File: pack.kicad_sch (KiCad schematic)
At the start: 34 parts

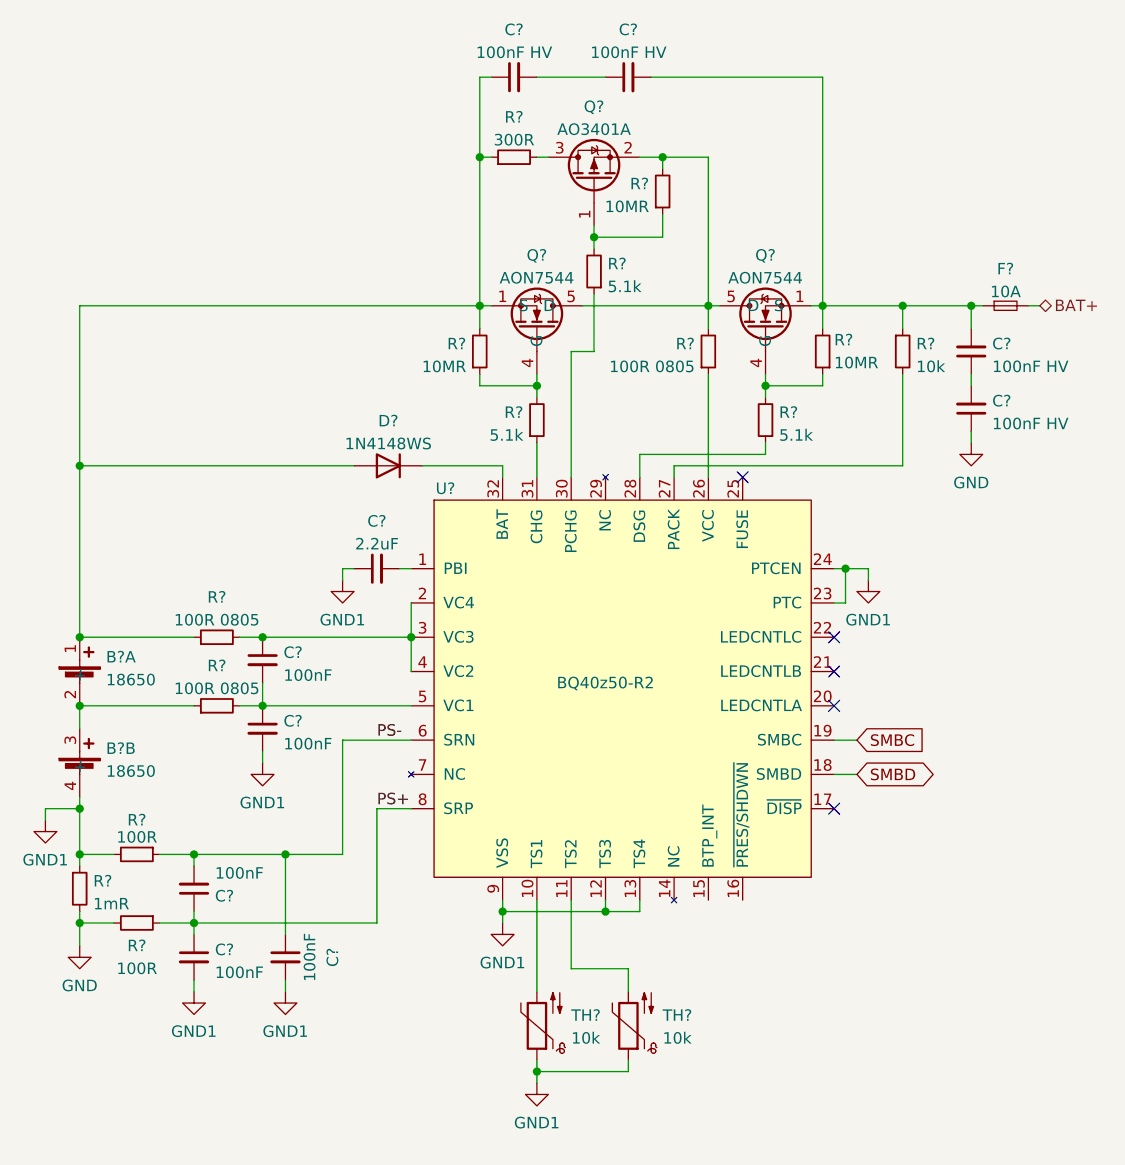
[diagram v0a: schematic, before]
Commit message: Add individually switchable outputs
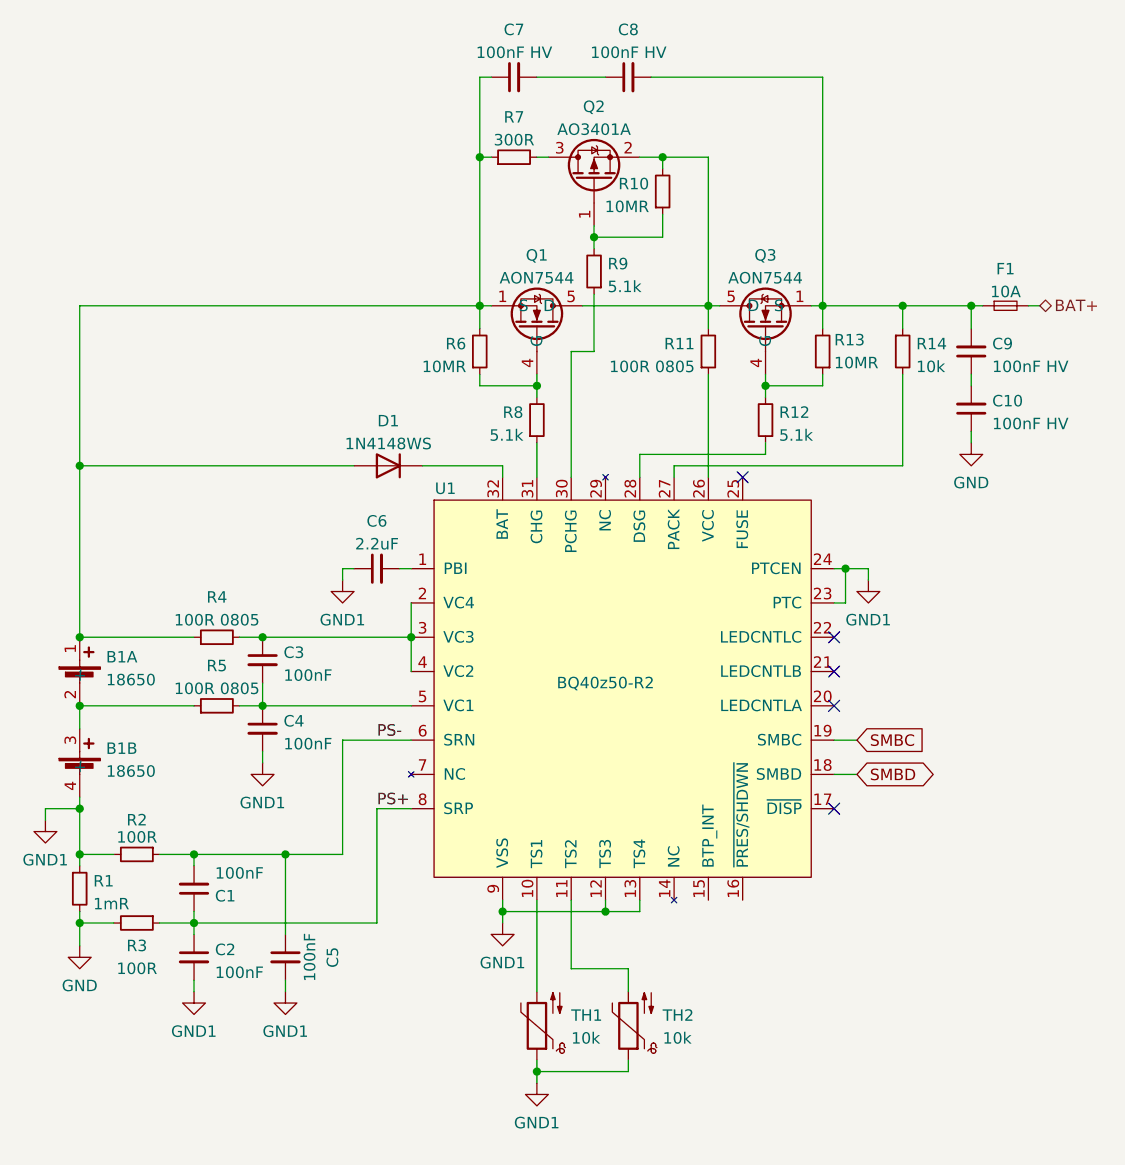
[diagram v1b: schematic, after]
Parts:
- gave numbers to parts that had none: 33

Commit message: Finish step-up component placement and partial layout
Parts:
- added R95: 10k, Resistor_SMD:R_0402_1005Metric, symbol Device:R_Small
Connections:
- net GND1: now also R95.2
- net at U1.16 (~{PRES/SHDWN}): now also R95.1
- no-connect marks 5 -> 6
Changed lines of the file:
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@@
   (no_connect (at 158.75 118.11))
   (no_connect (at 148.59 81.28))
+  (no_connect (at 144.78 128.27))
   (no_connect (at 158.75 99.06))
   (no_connect (at 158.75 106.68))
@@
     (stroke (width 0) (type default) (color 0 0 0 0))
   )
+  (wire (pts (xy 148.59 128.27) (xy 148.59 129.54))
+    (stroke (width 0) (type default) (color 0 0 0 0))
+  )
   (wire (pts (xy 121.92 80.01) (xy 121.92 81.28))
     (stroke (width 0) (type default) (color 0 0 0 0))
@@
   )
   (wire (pts (xy 87.63 137.16) (xy 87.63 138.43))
+    (stroke (width 0) (type default) (color 0 0 0 0))
+  )
+  (wire (pts (xy 148.59 134.62) (xy 148.59 135.89))
     (stroke (width 0) (type default) (color 0 0 0 0))
   )
@@
   (hierarchical_label "BAT+" (shape bidirectional) (at 181.61 62.23 0)
     (effects (font (size 1.27 1.27)) (justify left))
+  )
+  (symbol (lib_id "Device:R_Small") (at 148.59 132.08 0) (unit 1)
+    (in_bom yes) (on_board yes) (fields_autoplaced)
+    (property "Reference" "R95" (id 0) (at 150.0886 131.2453 0)
+      (effects (font (size 1.27 1.27)) (justify left))
+    )
+    (property "Value" "10k" (id 1) (at 150.0886 133.7822 0)
+      (effects (font (size 1.27 1.27)) (justify left))
+    )
+    (property "Footprint" "Resistor_SMD:R_0402_1005Metric" (id 2) (at 148.59 132.08 0)
+      (effects (font (size 1.27 1.27)) hide)
+    )
+    (property "Datasheet" "~" (id 3) (at 148.59 132.08 0)
+      (effects (font (size 1.27 1.27)) hide)
+    )
+    (property "LCSC" "C25744" (id 4) (at 148.59 132.08 0)
+      (effects (font (size 1.27 1.27)) hide)
+    )
+    (pin "1")
+    (pin "2")
   )
   (symbol (lib_id "power:GND1") (at 162.56 92.71 0) (unit 1)
@@
     (pin "4")
   )
+  (symbol (lib_id "power:GND1") (at 148.59 135.89 0) (unit 1)
+    (in_bom yes) (on_board yes) (fields_autoplaced)
+    (property "Reference" "#PWR0286" (id 0) (at 148.59 142.24 0)
+      (effects (font (size 1.27 1.27)) hide)
+    )
+    (property "Value" "GND1" (id 1) (at 148.59 140.3334 0))
+    (property "Footprint" "" (id 2) (at 148.59 135.89 0)
+      (effects (font (size 1.27 1.27)) hide)
+    )
+    (property "Datasheet" "" (id 3) (at 148.59 135.89 0)
+      (effects (font (size 1.27 1.27)) hide)
+    )
+    (pin "1")
+  )
   (symbol (lib_id "Device:C_Small") (at 87.63 127 0) (mirror x) (unit 1)

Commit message: Partial layout
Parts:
- TH1, TH2: footprint Resistor_SMD:R_0805_2012Metric -> Resistor_SMD:R_0402_1005Metric; LCSC C316395 -> C279801
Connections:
- net B+: now reaches B1.1 (+), C7.1, D1.2 (A), Q1.1 (S), Q1.2 (S), Q1.3 (S), R4.1, R6.2, R7.1
- net VCOM: now reaches Q1.5 (D), Q1.6 (D), Q1.7 (D), Q1.8 (D), Q1.9 (D), Q2.2 (S), Q3.5 (D), Q3.6 (D), Q3.7 (D), Q3.8 (D), Q3.9 (D), R10.2, R11.2
- net VBAT: now reaches C8.2, C9.2, F1.1, Q3.1 (S), Q3.2 (S), Q3.3 (S), R13.2, R14.1
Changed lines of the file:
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@@
     (stroke (width 0) (type default) (color 0 0 0 0))
+  )
+  (label "VCOM" (at 138.43 62.23 0)
+    (effects (font (size 1.27 1.27)) (justify left bottom))
   )
   (label "PS-" (at 107.95 110.49 0)
@@
   )
   (label "PS+" (at 107.95 118.11 0)
+    (effects (font (size 1.27 1.27)) (justify left bottom))
+  )
+  (label "B+" (at 74.93 96.52 90)
+    (effects (font (size 1.27 1.27)) (justify left bottom))
+  )
+  (label "VBAT" (at 166.37 62.23 0)
     (effects (font (size 1.27 1.27)) (justify left bottom))
   )
@@
       (effects (font (size 1.27 1.27)) (justify right))
     )
-    (property "Footprint" "Resistor_SMD:R_0805_2012Metric" (id 2) (at 135.89 143.51 0)
+    (property "Footprint" "Resistor_SMD:R_0402_1005Metric" (id 2) (at 135.89 143.51 0)
       (effects (font (size 1.27 1.27)) hide)
     )
@@
       (effects (font (size 1.27 1.27)) hide)
     )
-    (property "LCSC" "C316395" (id 4) (at 135.89 142.24 0)
+    (property "LCSC" "C279801" (id 4) (at 135.89 142.24 0)
       (effects (font (size 1.27 1.27)) hide)
     )
@@
       (effects (font (size 1.27 1.27)) (justify right))
     )
-    (property "Footprint" "Resistor_SMD:R_0805_2012Metric" (id 2) (at 125.73 143.51 0)
+    (property "Footprint" "Resistor_SMD:R_0402_1005Metric" (id 2) (at 125.73 143.51 0)
       (effects (font (size 1.27 1.27)) hide)
     )
@@
       (effects (font (size 1.27 1.27)) hide)
     )
-    (property "LCSC" "C316395" (id 4) (at 125.73 142.24 0)
-      (effects (font (size 1.27 1.27)) hide)
-    )
+    (property "LCSC" "C279801" (id 4) (at 125.73 142.24 0)
+      (effects (font (size 1.27 1.27)) hide)
+    )

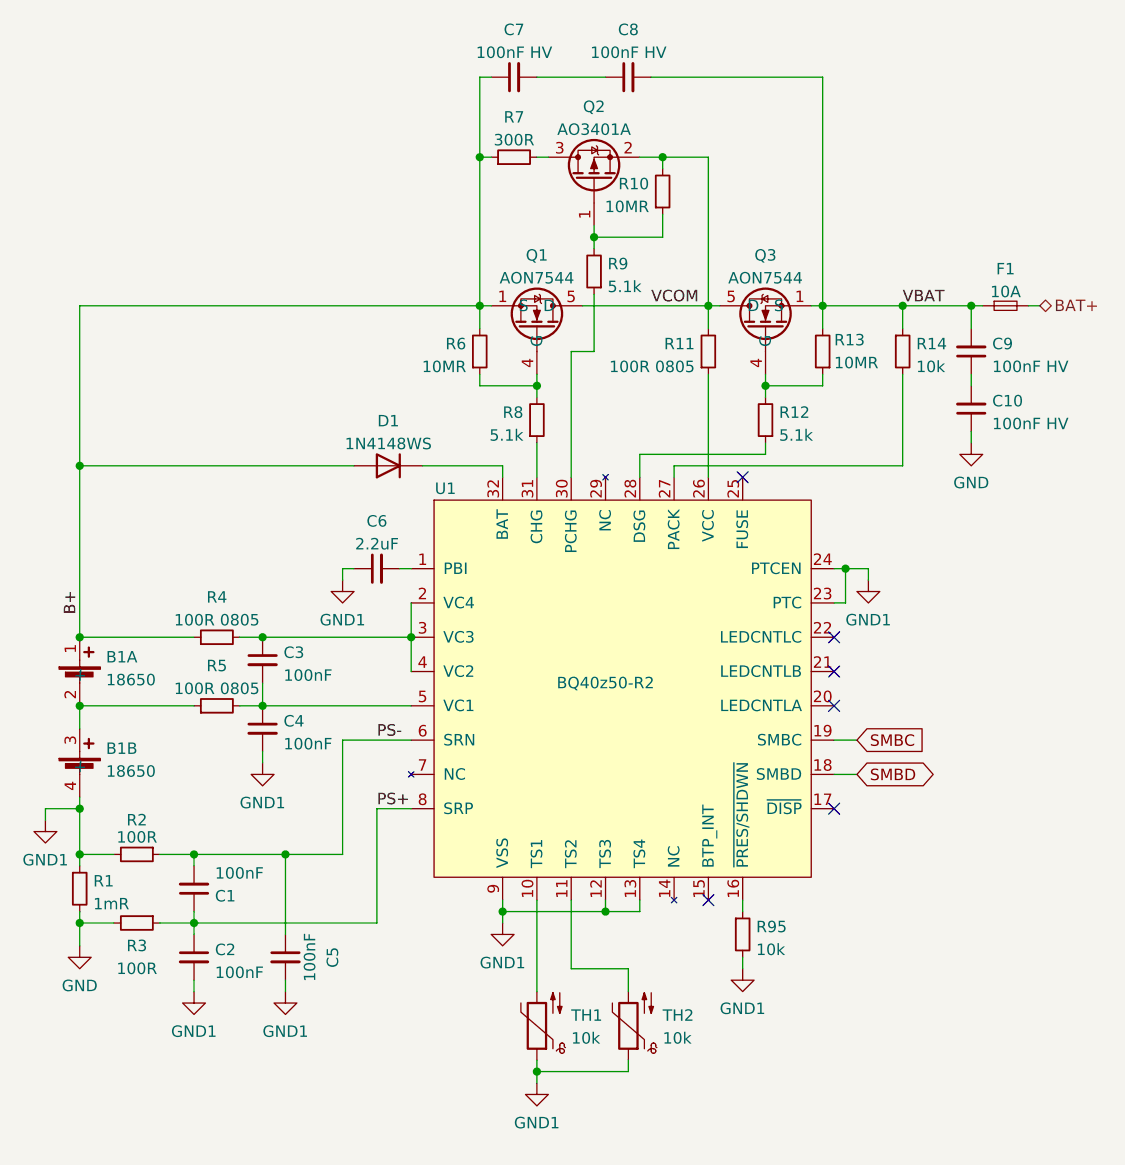
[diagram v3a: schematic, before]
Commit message: Add FUSE pulldown and PTC dummy
In contrast to documentation provided by TI FUSE is neither just an
output nor does the PTCEN feature work as advertised.

The FUSE pin contains a switchable 150nA current source. Presumably it
is used as a safety to detect if the FUSE pin is open. Unfortunately the
gauage will not allow control of the CHG, DSG and PRECHG FETs when it
detects an open FUSE pin. There does not seem to be any configuration
option for this behaviour either.

The PTC pin allows connecting a PTC to detect overheating of the main
power path control FETs. According to the BQ40Z50 datasheet it is possible
to disable this safety function by tieing PTCEN to VSS. Unfortunately this
does not seem to work as intended. When tieing both PTCEN and PTC to VSS
the gauage does not give any indication of a failure but refuses to switch
any of CHG, PRECHG or DSG FETs.
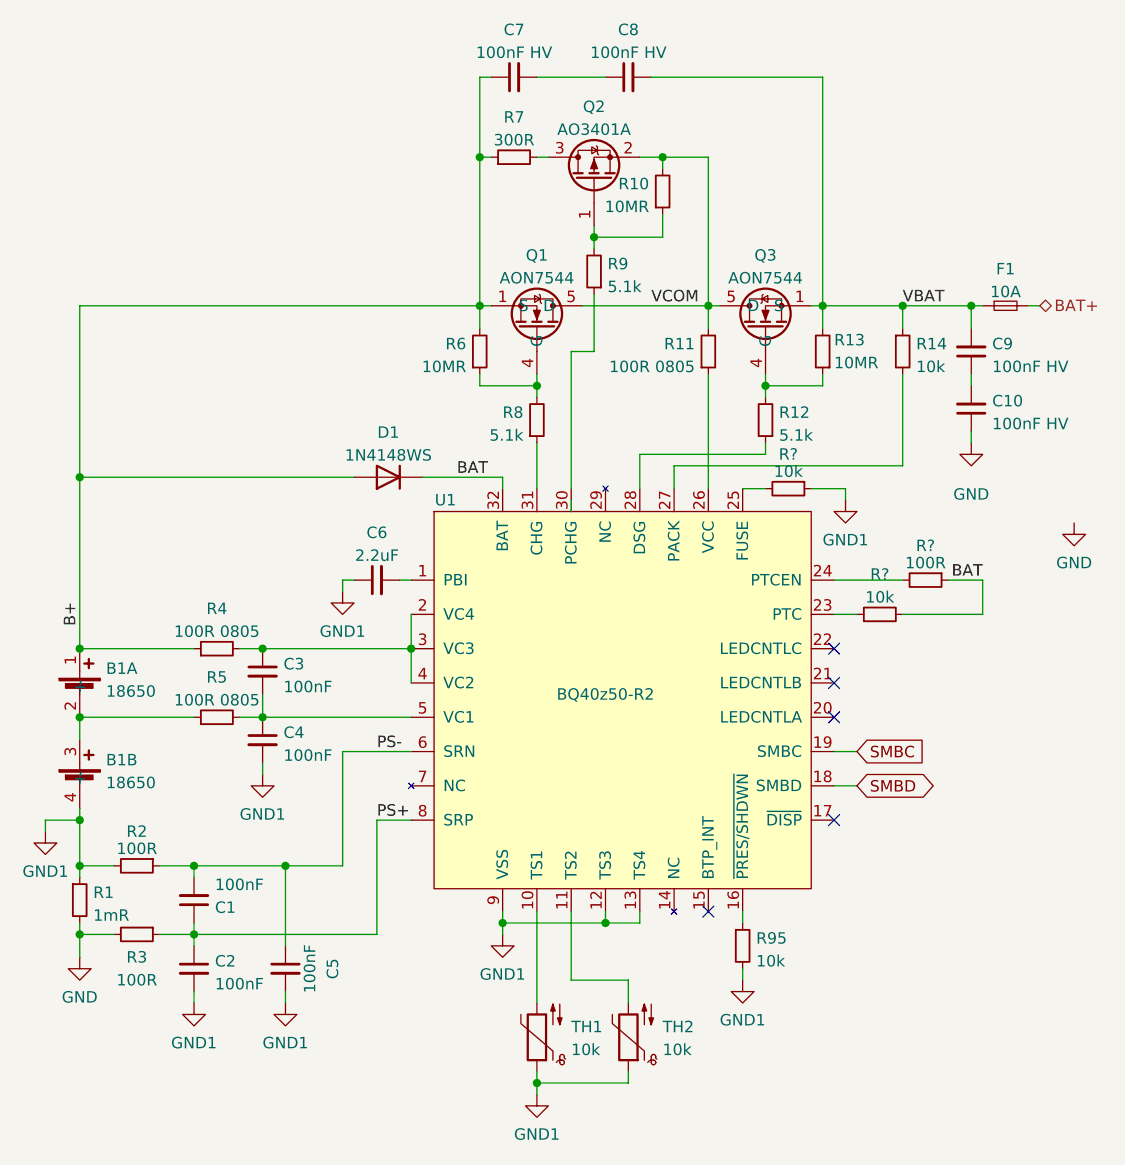
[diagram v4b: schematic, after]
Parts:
- added R? (x2): 10k, Resistor_SMD:R_0402_1005Metric, symbol Device:R_Small
- added R?: 100R, Resistor_SMD:R_0402_1005Metric, symbol Device:R_Small
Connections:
- net GND1: now also R?.1; no longer U1.23 (PTC), U1.24 (PTCEN)
- net at U1.25 (FUSE): now also R?.2
- net BAT: now reaches D1.1 (K), U1.32 (BAT)
- net BAT: now also R?.1, R?.2
- new net: R?.1, U1.23 (PTC)
- new net: R?.2, U1.24 (PTCEN)
- no-connect marks 6 -> 5
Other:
- moved on the sheet: B1A, B1B, C1, C2, C3, C4, C5, C6, D1, R1, R2, R3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

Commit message: Fix gate discharge resistor on Q10
The gate discharge resistor on Q10 was by mistake connected to drain
instead of source.
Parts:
- gave numbers to parts that had none: 3
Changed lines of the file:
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@@
   (symbol (lib_id "power:GND1") (at 160.02 83.82 0) (unit 1)
     (in_bom yes) (on_board yes) (fields_autoplaced)
-    (property "Reference" "#PWR?" (id 0) (at 160.02 90.17 0)
+    (property "Reference" "#PWR0316" (id 0) (at 160.02 90.17 0)
       (effects (font (size 1.27 1.27)) hide)
     )
@@
   (symbol (lib_id "power:GND") (at 185.42 86.36 0) (unit 1)
     (in_bom yes) (on_board yes) (fields_autoplaced)
-    (property "Reference" "#PWR?" (id 0) (at 185.42 92.71 0)
+    (property "Reference" "#PWR0109" (id 0) (at 185.42 92.71 0)
       (effects (font (size 1.27 1.27)) hide)
     )
@@
   (symbol (lib_id "Device:R_Small") (at 163.83 96.52 90) (unit 1)
     (in_bom yes) (on_board yes) (fields_autoplaced)
-    (property "Reference" "R?" (id 0) (at 163.83 92.0836 90))
+    (property "Reference" "R129" (id 0) (at 163.83 92.0836 90))
     (property "Value" "10k" (id 1) (at 163.83 94.6205 90))
     (property "Footprint" "Resistor_SMD:R_0402_1005Metric" (id 2) (at 163.83 96.52 0)
@@
   (symbol (lib_id "Device:R_Small") (at 168.91 92.71 270) (unit 1)
     (in_bom yes) (on_board yes)
-    (property "Reference" "R?" (id 0) (at 168.91 88.9 90))
+    (property "Reference" "R130" (id 0) (at 168.91 88.9 90))
     (property "Value" "100R" (id 1) (at 168.91 90.8105 90))
     (property "Footprint" "Resistor_SMD:R_0402_1005Metric" (id 2) (at 168.91 92.71 0)
@@
   (symbol (lib_id "Device:R_Small") (at 153.67 82.55 270) (unit 1)
     (in_bom yes) (on_board yes)
-    (property "Reference" "R?" (id 0) (at 153.67 78.74 90))
+    (property "Reference" "R128" (id 0) (at 153.67 78.74 90))
     (property "Value" "10k" (id 1) (at 153.67 80.6505 90))
     (property "Footprint" "Resistor_SMD:R_0402_1005Metric" (id 2) (at 153.67 82.55 0)
